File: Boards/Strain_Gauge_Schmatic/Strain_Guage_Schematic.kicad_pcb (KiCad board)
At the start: 2 copper layers, 32 x 17 mm, 21 parts, among them J1 Conn_01x03_Male, J2 Conn_01x02_Male, U1 LM358

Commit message: Added order number to strain guage schematic
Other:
- board text added: "JLCJLCJLCJLC"

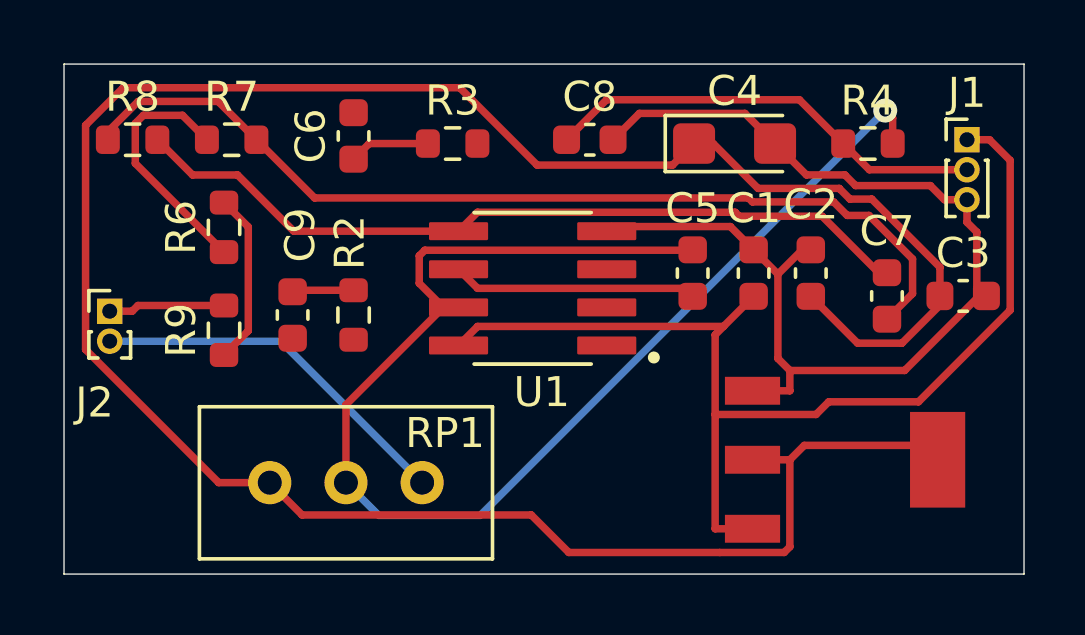
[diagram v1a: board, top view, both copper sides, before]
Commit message: Small error in strain gauge schematic, C4 footprint a bit big
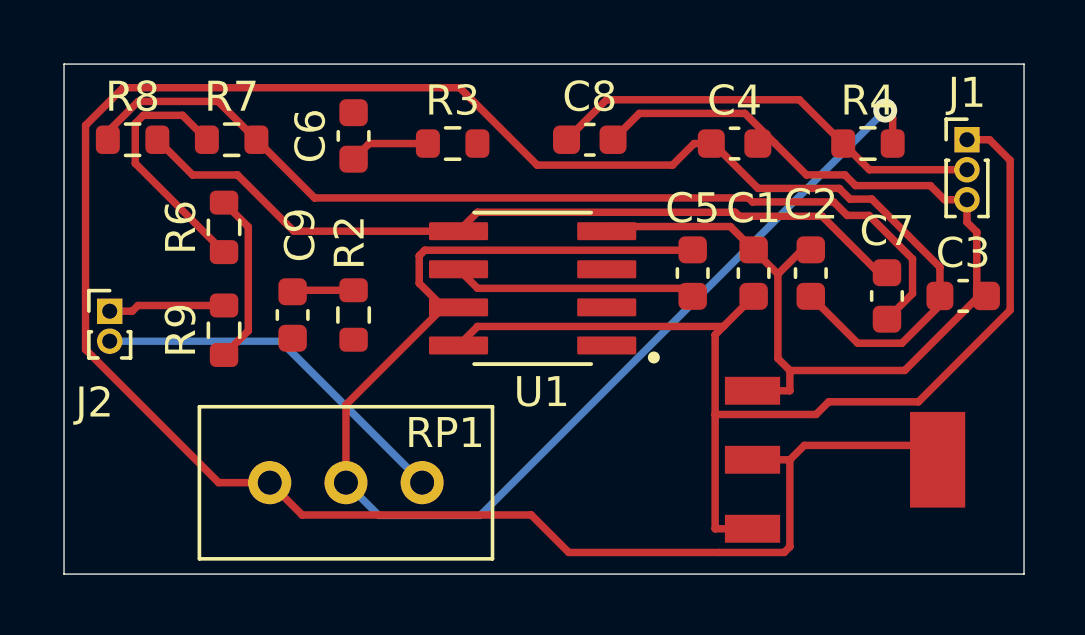
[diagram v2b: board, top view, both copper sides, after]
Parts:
- C4: footprint Capacitor_Tantalum_SMD:CP_EIA-3216-18_Kemet-A -> Capacitor_SMD:C_0603_1608Metric
- C5, C6, C7, C8, C9: value C -> 100nF
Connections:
- U1 pad 4: GND -> (no net)
- U1 pad 8: /Regulator/Vcc -> (no net)
